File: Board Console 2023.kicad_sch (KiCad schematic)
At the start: 33 parts, among them J1 Raspberry PI, J2 Composite OUT, J3 L1/L2, J5 USB_B_Micro, J6 Display, J7 USB_A, J8 R1/R2, SW10 A, SW11 X, SW12 Down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

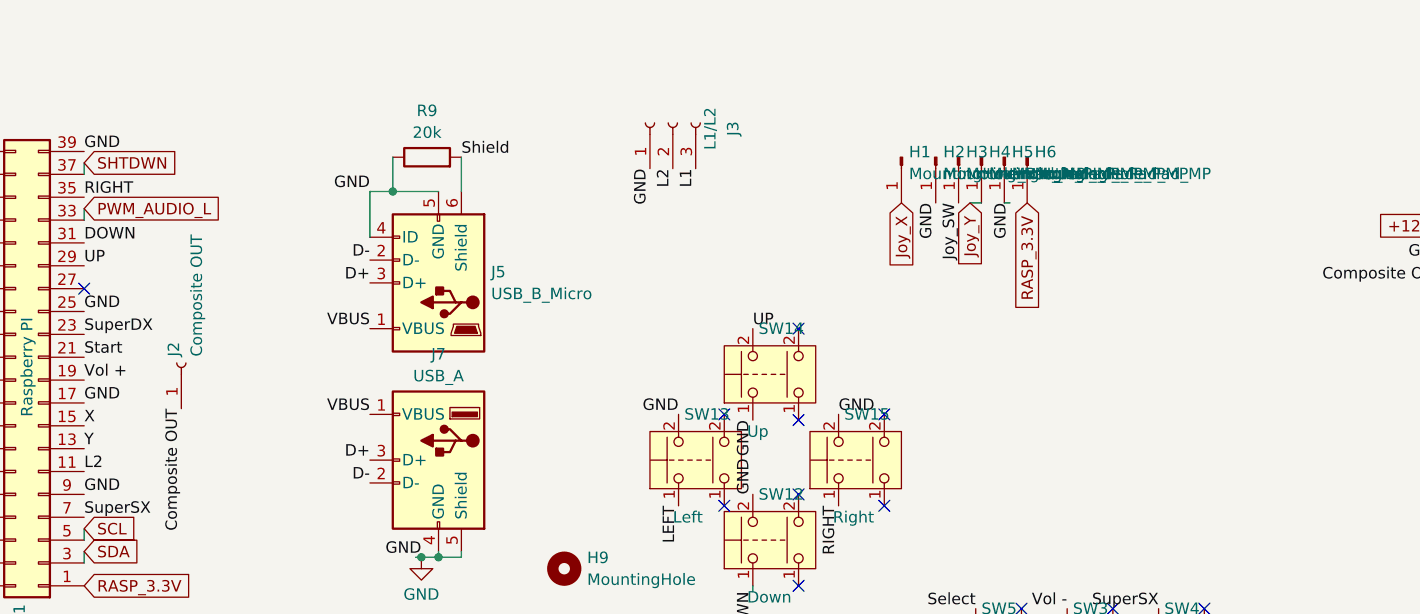
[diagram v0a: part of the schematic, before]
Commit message: fix hdmi traces and push button kill pin supply
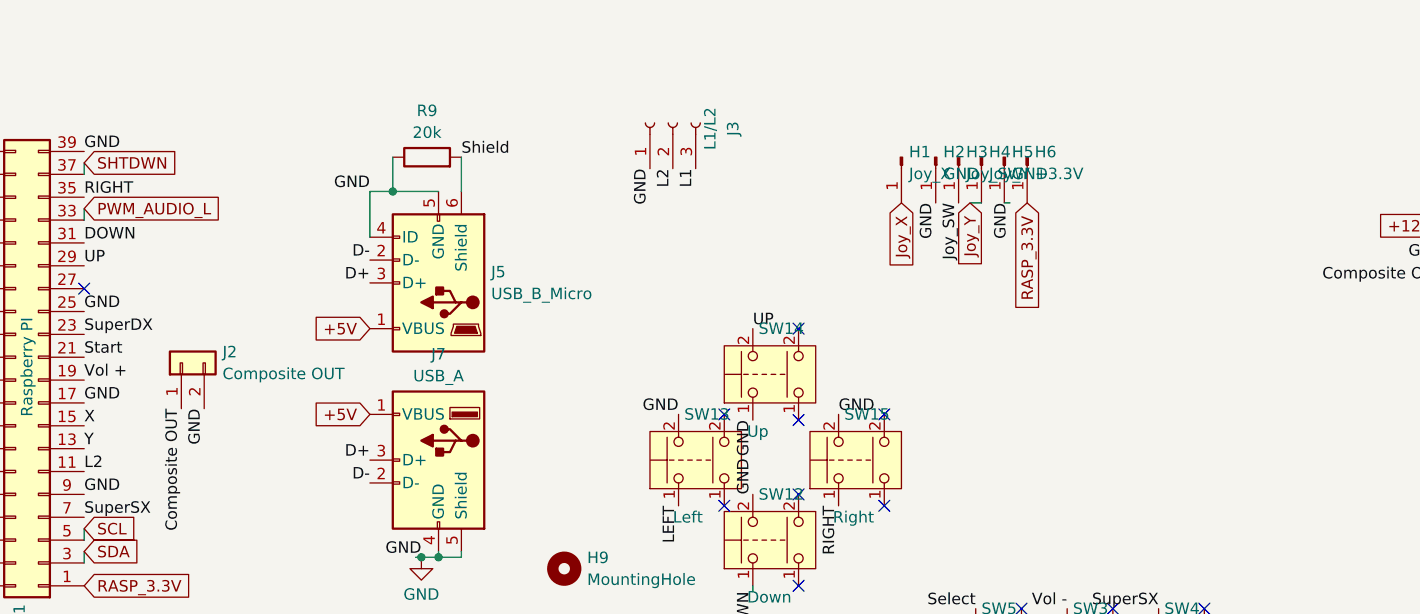
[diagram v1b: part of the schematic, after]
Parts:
- H1: value MountingHole_Pad_MP -> Joy_X
- H2, H5: value MountingHole_Pad_MP -> GND
- H3: value MountingHole_Pad_MP -> Joy_SW
- H4: value MountingHole_Pad_MP -> Joy_Y
- H6: value MountingHole_Pad_MP -> +3.3V
- J2: footprint Connector_PinHeader_2.54mm:PinHeader_1x01_P2.54mm_Vertical -> Connector_PinHeader_2.00mm:PinHeader_1x02_P2.00mm_Vertical; symbol Connector:Conn_01x01_Female -> Connector_Generic:Conn_01x02
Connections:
- net VBUS is gone; now on net +5V: J5.1 (VBUS), J7.1 (VBUS)
- net GND: now also J2.2 (Pin_2)
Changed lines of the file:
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@@
 	)
 	(label "GND"
+		(at 99.695 123.825 270)
+		(fields_autoplaced yes)
+		(effects
+			(font
+				(size 1.27 1.27)
+			)
+			(justify right bottom)
+		)
+	)
+	(label "GND"
 		(at 316.865 91.44 0)
 		(fields_autoplaced yes)
@@
 		)
 	)
-	(label "VBUS"
-		(at 118.11 114.935 180)
-		(fields_autoplaced yes)
-		(effects
-			(font
-				(size 1.27 1.27)
-			)
-			(justify right bottom)
-		)
-	)
 	(label "SuperDX"
 		(at 86.36 115.57 0)
@@
 		)
 	)
-	(label "VBUS"
-		(at 118.11 124.46 180)
-		(fields_autoplaced yes)
-		(effects
-			(font
-				(size 1.27 1.27)
-			)
-			(justify right bottom)
-		)
-	)
 	(label "GND"
 		(at 86.36 95.25 0)
@@
 		)
 	)
+	(global_label "+5V"
+		(shape input)
+		(at 118.11 114.935 180)
+		(fields_autoplaced yes)
+		(effects
+			(font
+				(size 1.27 1.27)
+			)
+			(justify right)
+		)
+		(property "Intersheetrefs" "${INTERSHEET_REFS}"
+			(at 111.2543 114.935 0)
+			(effects
+				(font
+					(size 1.27 1.27)
+				)
+				(justify right)
+				(hide yes)
+			)
+		)
+	)
 	(global_label "SHTDWN"
 		(shape input)
@@
 		)
 	)
+	(global_label "+5V"
+		(shape input)
+		(at 118.11 124.46 180)
+		(fields_autoplaced yes)
+		(effects
+			(font
+				(size 1.27 1.27)
+			)
+			(justify right)
+		)
+		(property "Intersheetrefs" "${INTERSHEET_REFS}"
+			(at 111.2543 124.46 0)
+			(effects
+				(font
+					(size 1.27 1.27)
+				)
+				(justify right)
+				(hide yes)
+			)
+		)
+	)
 	(global_label "SCL"
 		(shape input)
@@
 			)
 		)
-		(property "Value" "MountingHole_Pad_MP"
+		(property "Value" "GND"
 			(at 181.8132 97.7321 90)
 			(effects
@@
 			)
 		)
-		(property "Value" "MountingHole_Pad_MP"
+		(property "Value" "Joy_Y"
 			(at 186.8932 97.7321 90)
 			(effects
@@
 			)
 		)
-		(property "Value" "MountingHole_Pad_MP"
+		(property "Value" "+3.3V"
 			(at 191.9732 97.7321 90)
 			(effects
@@
 			)
 		)
-		(property "Value" "MountingHole_Pad_MP"
+		(property "Value" "Joy_SW"
 			(at 184.3532 97.7321 90)
 			(effects
@@
 	)
 	(symbol
-		(lib_name "SwitchMod:SW_Push_Dual")
 		(lib_id "SwitchMod:SW_Push_Dual")
 		(at 154.94 129.54 90)
@@
 	)
 	(symbol
-		(lib_id "Connector:Conn_01x01_Female")
+		(lib_id "Connector_Generic:Conn_01x02")
 		(at 97.155 118.745 90)
 		(unit 1)
@@
 		(fields_autoplaced yes)
 		(property "Reference" "J2"
-			(at 96.3203 118.0338 0)
+			(at 101.727 117.5328 90)
 			(effects
 				(font
 					(size 1.27 1.27)
 				)
-				(justify left)
+				(justify right)
 			)
 		)
 		(property "Value" "Composite OUT"
-			(at 98.8572 118.0338 0)
+			(at 101.727 119.9571 90)
 			(effects
 				(font
 					(size 1.27 1.27)
 				)
-				(justify left)
+				(justify right)
 			)
 		)
-		(property "Footprint" "Connector_PinHeader_2.54mm:PinHeader_1x01_P2.54mm_Vertical"
+		(property "Footprint" "Connector_PinHeader_2.00mm:PinHeader_1x02_P2.00mm_Vertical"
 			(at 97.155 118.745 0)
 			(effects
@@
 			)
 		)
-		(property "Description" ""
+		(property "Description" "Generic connector, single row, 01x02, script generated (kicad-library-utils/schlib/autogen/connector/)"
 			(at 97.155 118.745 0)
 			(effects
@@
 		(pin "1"
 		)
+		(pin "2"
+		)
 		(instances
 			(project "Board Console 2023"
@@
 			)
 		)
-		(property "Value" "MountingHole_Pad_MP"
+		(property "Value" "GND"
 			(at 189.4332 97.7321 90)
 			(effects
@@
 			)
 		)
-		(property "Value" "MountingHole_Pad_MP"
+		(property "Value" "Joy_X"
 			(at 178.0032 97.7321 90)
 			(effects

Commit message: update layout pcb & zip tesi
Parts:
- added JP7: SJ, Jumper:SolderJumper-2_P1.3mm_Open_Pad1.0x1.5mm, symbol Jumper:SolderJumper_2_Open
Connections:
- net GND: now also JP7.1 (A); no longer J7.5 (Shield)
- new net: J7.5 (Shield), JP7.2 (B)
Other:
- moved on the sheet: H10, H11, H13, H8, H9, J1, J2, J3, J5, J6, J7, J8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

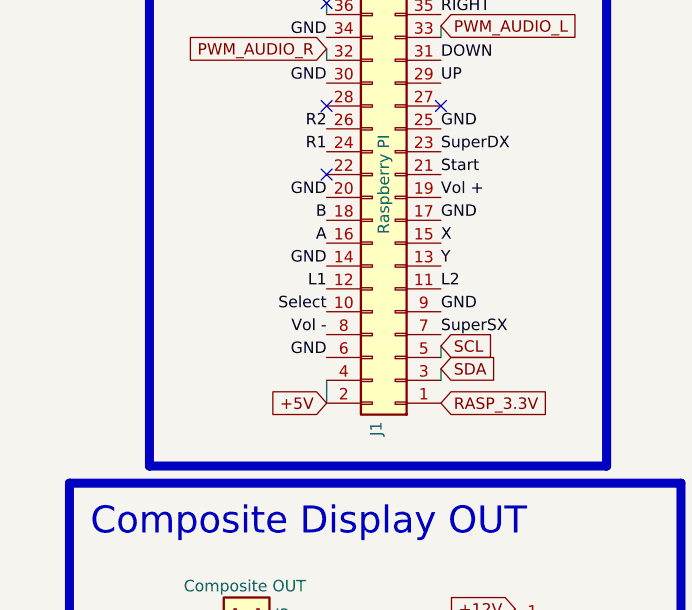
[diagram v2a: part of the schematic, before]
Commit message: aggiunto pin enable switch per schermo composito
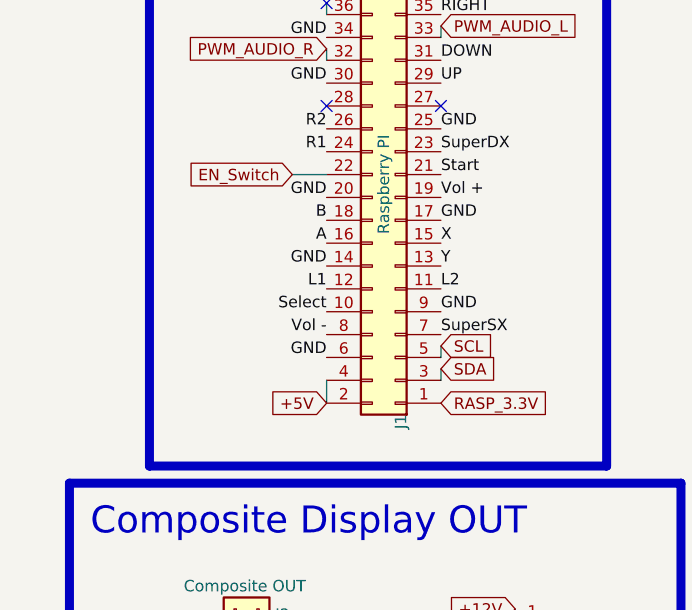
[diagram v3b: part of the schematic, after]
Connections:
- net EN_Switch: now reaches J1.22 (Pin_22)
- no-connect marks 32 -> 31
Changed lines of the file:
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@@
 	)
 	(no_connect
-		(at 52.07 99.06)
-	)
-	(no_connect
 		(at 179.07 90.17)
 	)
@@
 	(wire
 		(pts
+			(xy 48.26 99.06) (xy 52.07 99.06)
+		)
+		(stroke
+			(width 0)
+			(type default)
+		)
+	)
+	(wire
+		(pts
 			(xy 52.07 80.01) (xy 52.07 81.28)
 		)
@@
 		)
 	)
+	(global_label "EN_Switch"
+		(shape input)
+		(at 48.26 99.06 180)
+		(fields_autoplaced yes)
+		(effects
+			(font
+				(size 1.27 1.27)
+			)
+			(justify right)
+		)
+		(property "Intersheetrefs" "${INTERSHEET_REFS}"
+			(at 35.7196 99.06 0)
+			(effects
+				(font
+					(size 1.27 1.27)
+				)
+				(justify right)
+				(hide yes)
+			)
+		)
+	)
 	(global_label "SHTDWN"
 		(shape input)
@@
 	)
 	(symbol
-		(lib_name "SwitchMod:SW_Push_Dual")
 		(lib_id "SwitchMod:SW_Push_Dual")
 		(at 176.53 95.25 90)
@@
 	)
 	(symbol
-		(lib_name "SwitchMod:SW_Push_Dual")
 		(lib_id "SwitchMod:SW_Push_Dual")
 		(at 243.84 107.95 90)
@@
 	)
 	(symbol
-		(lib_name "SwitchMod:SW_Push_Dual")
 		(lib_id "SwitchMod:SW_Push_Dual")
 		(at 186.69 107.95 90)
@@
 	)
 	(symbol
-		(lib_name "SwitchMod:SW_Push_Dual")
 		(lib_id "SwitchMod:SW_Push_Dual")
 		(at 191.135 137.16 90)
@@
 	)
 	(symbol
-		(lib_name "SwitchMod:SW_Push_Dual")
 		(lib_id "SwitchMod:SW_Push_Dual")
 		(at 233.68 121.285 90)
@@
 	)
 	(symbol
-		(lib_name "SwitchMod:SW_Push_Dual")
 		(lib_id "SwitchMod:SW_Push_Dual")
 		(at 233.68 95.25 90)
@@
 	)
 	(symbol
-		(lib_name "SwitchMod:SW_Push_Dual")
 		(lib_id "SwitchMod:SW_Push_Dual")
 		(at 223.52 107.95 90)
@@
 	)
 	(symbol
-		(lib_name "SwitchMod:SW_Push_Dual")
 		(lib_id "SwitchMod:SW_Push_Dual")
 		(at 166.37 107.95 90)
@@
 	)
 	(symbol
-		(lib_name "SwitchMod:SW_Push_Dual")
 		(lib_id "SwitchMod:SW_Push_Dual")
 		(at 210.185 137.16 90)
@@
 	)
 	(symbol
-		(lib_name "SwitchMod:SW_Push_Dual")
 		(lib_id "SwitchMod:SW_Push_Dual")
 		(at 175.895 121.285 90)
@@
 	)
 	(symbol
-		(lib_name "SwitchMod:SW_Push_Dual")
 		(lib_id "SwitchMod:SW_Push_Dual")
 		(at 175.26 137.16 90)
@@
 	)
 	(symbol
-		(lib_name "SwitchMod:SW_Push_Dual")
 		(lib_id "SwitchMod:SW_Push_Dual")
 		(at 159.385 137.16 90)
@@
 		(dnp no)
 		(property "Reference" "J1"
-			(at 57.5853 126.492 90)
+			(at 60.325 125.73 90)
 			(effects
 				(font
@@
 	)
 	(symbol
-		(lib_name "SwitchMod:SW_Push_Dual")
 		(lib_id "SwitchMod:SW_Push_Dual")
 		(at 241.935 137.16 90)
@@
 	)
 	(symbol
-		(lib_name "SwitchMod:SW_Push_Dual")
 		(lib_id "SwitchMod:SW_Push_Dual")
 		(at 226.06 137.16 90)
